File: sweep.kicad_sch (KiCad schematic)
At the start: 208 parts, among them J1 USB_C_Receptacle_USB2.0_16P, J10 Conn_01x12, J11 Conn_01x01, J12 Conn_01x01, J13 Conn_01x01, J2 Conn_01x01, J3 USB_C_Receptacle_USB2.0_16P, J4 USB_C_Receptacle_USB2.0_16P, J5 USB_C_Receptacle_USB2.0_16P, J7 Conn_01x05, J8 Conn_01x05, J9 Conn_01x12, SW1 SW_Push, SW10 SW_Push, SW11 SW_Push, SW12 SW_Push, SW13 SW_Push, SW14 SW_Push, SW15 SW_Push, SW16 SW_Push, SW17 SW_Push, SW18 SW_Push, SW19 SW_Push, SW2 SW_Push, SW20 SW_Push, SW21 SW_Push, SW22 SW_Push, SW23 SW_Push, SW24 SW_Push, SW25 SW_Push, SW26 SW_Push, SW27 SW_Push, SW28 SW_Push, SW29 SW_Push, SW3 SW_Push, SW30 SW_Push, SW31 SW_Push, SW32 SW_Push, SW33 SW_Push, SW34 SW_Push, SW35 SW_Push, SW36 SW_Push, SW37 SW_Push, SW38 SW_Push, SW4 SW_Push, SW5 SW_Push, SW6 SW_Push, SW7 SW_Push, SW8 SW_Push, SW9 SW_Push, U1 RP2040, U10 SN74LVC1T45DRL, U2 XC6206PxxxMR, U3 SRV05-4, U4 W25Q128JVS, U5 RP2040, U6 SRV05-4, U7 XC6206PxxxMR, U8 W25Q128JVS, U9 SN74LVC1T45DRL, Y1 Crystal_GND24, Y2 Crystal_GND24

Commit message: Adds updated PCBs (see changelog) and production files
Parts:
- removed J10, J9: Conn_01x12, PCM_marbastlib-various:CON_FH33J-12S-0.5SH, symbol Connector_Generic:Conn_01x12
- removed J7, J8: Conn_01x05, Connector_PinHeader_2.54mm:PinHeader_1x05_P2.54mm_Vertical, symbol Connector_Generic:Conn_01x05
- removed JP1, JP2, JP3, JP4: SolderJumper_2_Open, Jumper:SolderJumper-2_P1.3mm_Open_RoundedPad1.0x1.5mm, symbol Jumper:SolderJumper_2_Open
- added C75, C76: 100n, Capacitor_SMD:C_0402_1005Metric, symbol Device:C_Small
- added J6, J7: Conn_01x08, Connector_FFC-FPC:TE_0-1734839-8_1x08-1MP_P0.5mm_Horizontal, symbol Connector_Generic:Conn_01x08
- added R23, R26: 0.005, Resistor_SMD:R_1206_3216Metric, symbol Device:R_Small
- added R24, R25, R27, R28: 75k, Resistor_SMD:R_0402_1005Metric, symbol Device:R_Small
- added U11, U12: INA138, Package_TO_SOT_SMD:SOT-23-5, symbol Amplifier_Current:INA138
- J11, J12, J13, J2: now left out of the parts list
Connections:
- net MISO_L is gone; now on net LCD_CS_L: U1.7 (GPIO5)
- net MISO_R is gone; now on net LCD_CS_R: U5.7 (GPIO5)
- net +3V3: now also J6.7 (Pin_7), J7.7 (Pin_7)
- net +5V: now also C75.1, C76.1, R23.1, R24.1, R26.1, R27.1, U11.4 (-), U11.5 (V+), U12.4 (-), U12.5 (V+); no longer F1.2, F2.2
- net GND: now also C75.2, C76.2, J6.2 (Pin_2), J7.2 (Pin_2), R25.2, R28.2, U11.2 (GND), U12.2 (GND)
- net LCD_CS_L: now also J6.8 (Pin_8); no longer U1.9 (GPIO7)
- net LCD_CS_R: now also J7.8 (Pin_8); no longer U5.9 (GPIO7)
- net SW14_R: now also U5.35 (GPIO23); no longer U5.32 (GPIO21)
- net SW15_R: now also U5.34 (GPIO22); no longer U5.35 (GPIO23)
- net SW4_R: now also U5.32 (GPIO21); no longer U5.34 (GPIO22)
- net CURR_MEAS_R: now reaches U5.38 (GPIO26_ADC0)
- net CURR_MEAS_R: now also U12.1
- net VOLT_MEAS_R: now reaches U5.39 (GPIO27_ADC1)
- net VOLT_MEAS_R: now also R27.2, R28.1
- net LCD_RST_R: now reaches U5.40 (GPIO28_ADC2)
- net LCD_RST_R: now also J7.3 (Pin_3)
- net CURR_MEAS_L: now reaches U1.38 (GPIO26_ADC0)
- net CURR_MEAS_L: now also U11.1
- net VOLT_MEAS_L: now reaches U1.39 (GPIO27_ADC1)
- net VOLT_MEAS_L: now also R24.2, R25.1
- net LCD_RST_L: now reaches U1.40 (GPIO28_ADC2)
- net LCD_RST_L: now also J6.3 (Pin_3)
- net CIRQUE_CS_L renamed SPI_MISO_L
- net SPI_MISO_L: now also J6.4 (Pin_4)
- net CIRQUE_CS_R renamed SPI_MISO_R
- net SPI_MISO_R: now also J7.4 (Pin_4)
- net MOSI_L renamed SPI_MOSI_L
- net SPI_MOSI_L: now also J6.5 (Pin_5)
- net MOSI_R renamed SPI_MOSI_R
- net SPI_MOSI_R: now also J7.5 (Pin_5)
- net SCK_L renamed SPI_SCK_L
- net SPI_SCK_L: now also J6.6 (Pin_6)
- net SCK_R renamed SPI_SCK_R
- net SPI_SCK_R: now also J7.6 (Pin_6)
- new net: F1.2, R23.2, U11.3 (+)
- new net: F2.2, R26.2, U12.3 (+)
- new net LCD_BL_L: J6.1 (Pin_1), U1.9 (GPIO7)
- new net LCD_BL_R: J7.1 (Pin_1), U5.9 (GPIO7)
- no-connect marks 32 -> 20
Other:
- note added: "power symbols"
- moved on the sheet: C1, C10, C11, C12, C13, C14, C15, C16, C17, C18, C19, C2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

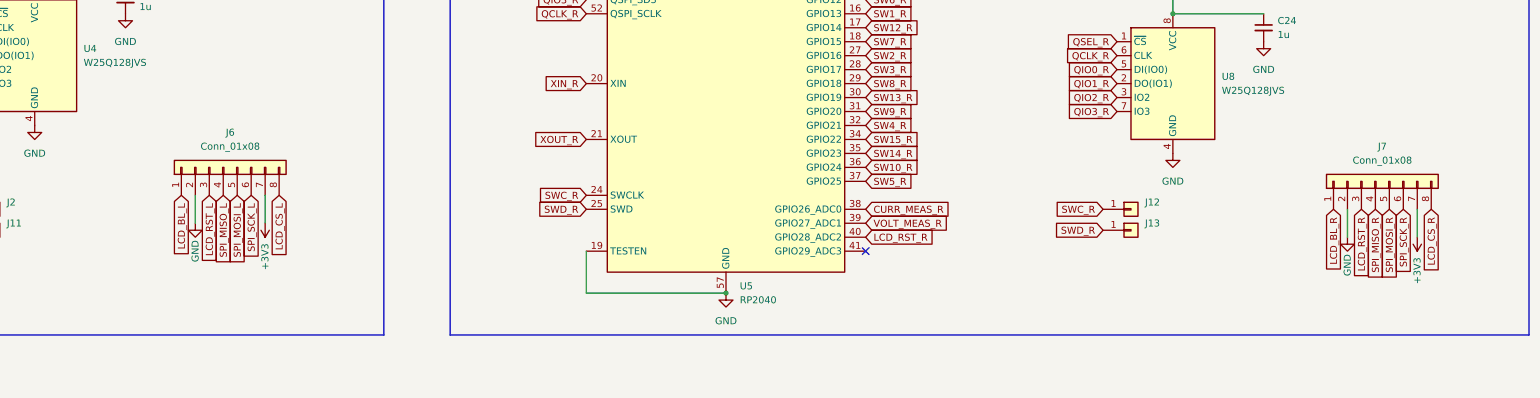
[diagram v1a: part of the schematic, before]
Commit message: Fix FPC connector pinout, minor readme syntax updates
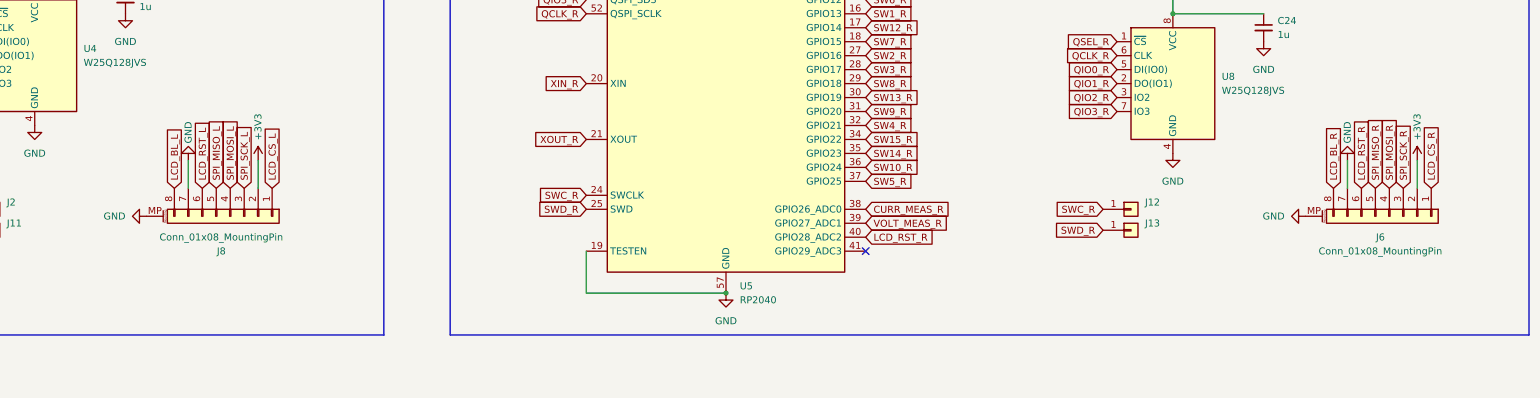
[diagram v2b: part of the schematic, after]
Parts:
- removed J6, J7: Conn_01x08, Connector_FFC-FPC:TE_0-1734839-8_1x08-1MP_P0.5mm_Horizontal, symbol Connector_Generic:Conn_01x08
- added J6, J8: Conn_01x08_MountingPin, Connector_FFC-FPC:TE_0-1734839-8_1x08-1MP_P0.5mm_Horizontal, symbol Connector_Generic_MountingPin:Conn_01x08_MountingPin
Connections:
- net +3V3: now also J6.2 (Pin_2), J8.2 (Pin_2)
- net GND: now also J6.7 (Pin_7), J6.MP (MountPin), J8.7 (Pin_7), J8.MP (MountPin)
- net LCD_BL_L: now also J8.8 (Pin_8)
- net LCD_BL_R: now also J6.8 (Pin_8)
- net LCD_CS_L: now also J8.1 (Pin_1)
- net LCD_CS_R: now also J6.1 (Pin_1)
- net LCD_RST_L: now also J8.6 (Pin_6)
- net LCD_RST_R: now also J6.6 (Pin_6)
- net SPI_MISO_L: now also J8.5 (Pin_5)
- net SPI_MISO_R: now also J6.5 (Pin_5)
- net SPI_MOSI_L: now also J8.4 (Pin_4)
- net SPI_MOSI_R: now also J6.4 (Pin_4)
- net SPI_SCK_L: now also J8.3 (Pin_3)
- net SPI_SCK_R: now also J6.3 (Pin_3)
